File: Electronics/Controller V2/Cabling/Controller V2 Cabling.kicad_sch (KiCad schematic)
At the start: 16 parts, among them J1 776164-1, J10 Autosteer Motor, J11 Battery, J12 776286-1, J13 WAS, J2 GPIO, J3 Tractor CAN, J4 Scraper CAN, J5 Spare CAN, J6 Front Height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

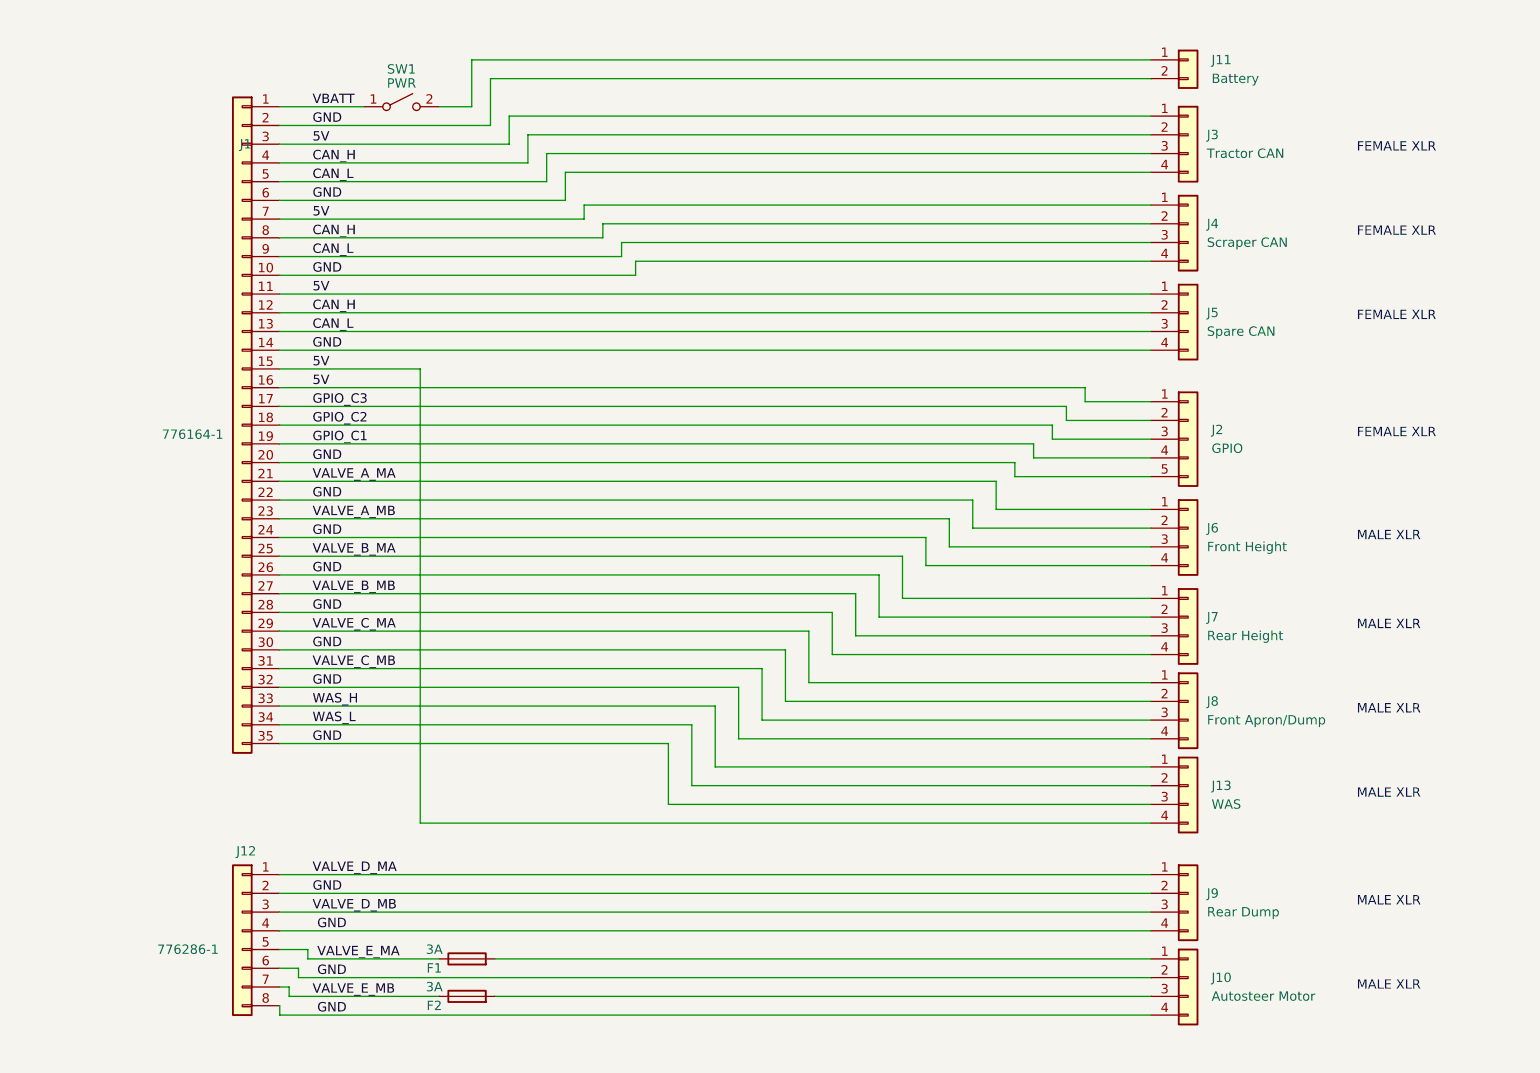
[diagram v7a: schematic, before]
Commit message: Updated controller V2 cabling. Added additional IMU PGNs - not currently used.
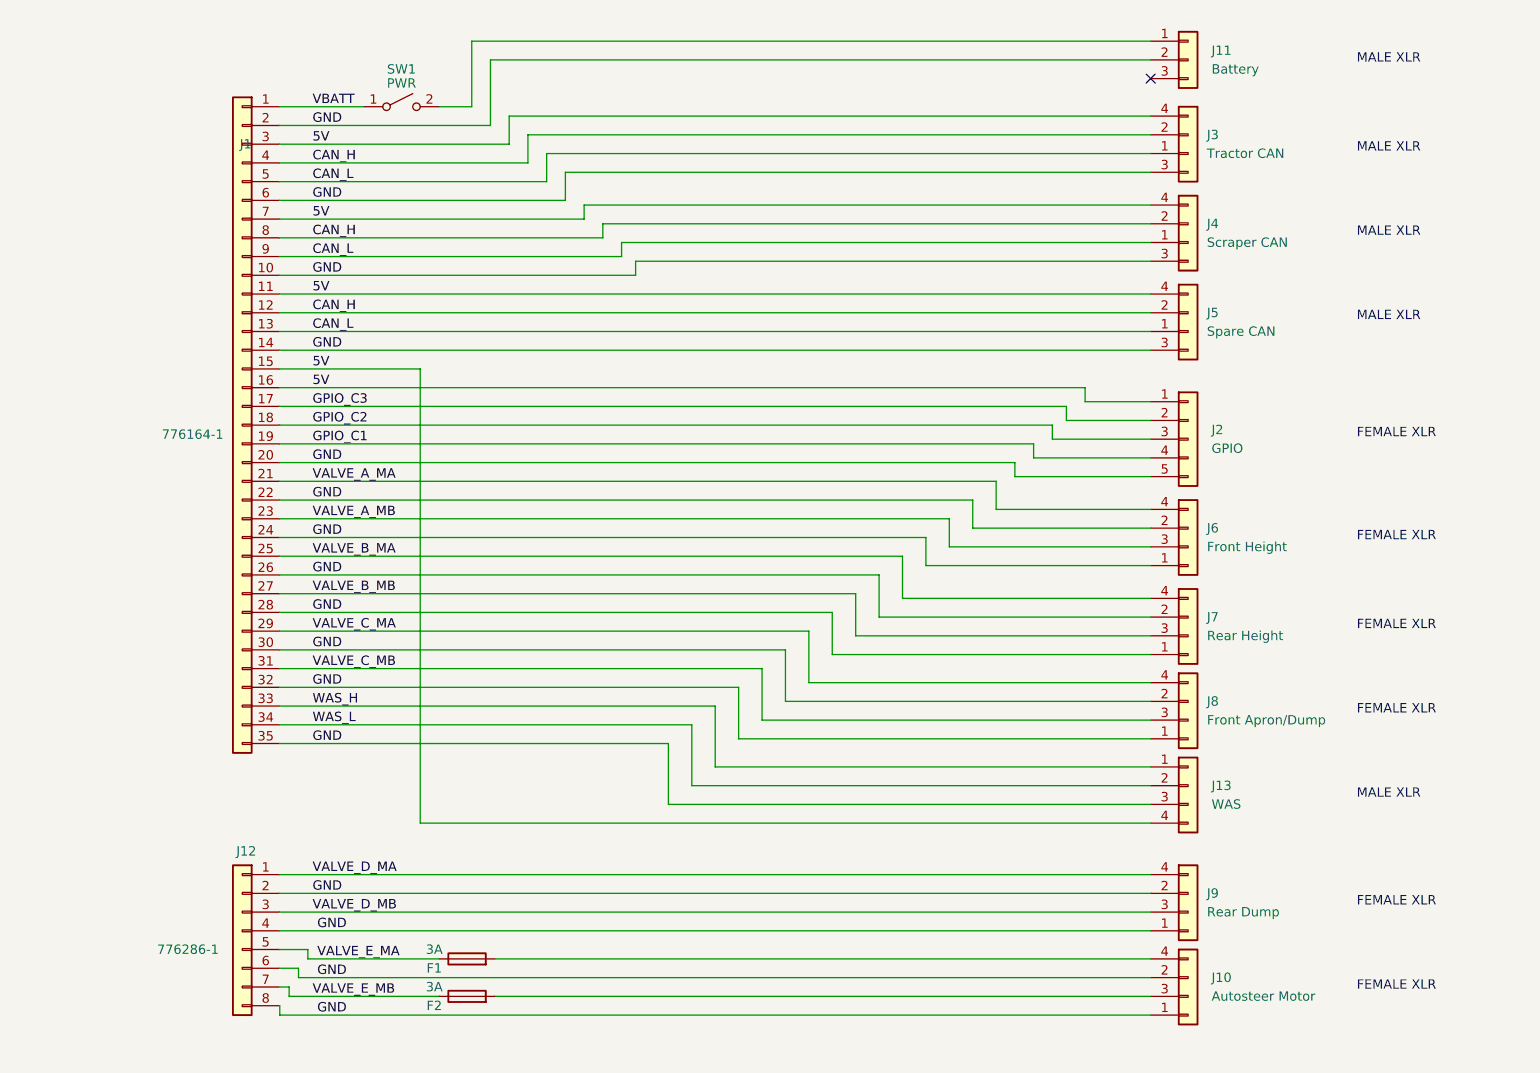
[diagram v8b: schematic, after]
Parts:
- J11: symbol Connector_Generic:Conn_01x02 -> Connector_Generic:Conn_01x03
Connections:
- net 5V: now also J3.4 (Pin_1), J4.4 (Pin_1), J5.4 (Pin_1); no longer J3.1 (Pin_1), J4.1 (Pin_1), J5.1 (Pin_1)
- net CAN_L: now also J3.1 (Pin_3), J4.1 (Pin_3), J5.1 (Pin_3); no longer J3.3 (Pin_3), J4.3 (Pin_3), J5.3 (Pin_3)
- net GND: now also J10.1 (Pin_4), J3.3 (Pin_4), J4.3 (Pin_4), J5.3 (Pin_4), J6.1 (Pin_4), J7.1 (Pin_4), J8.1 (Pin_4), J9.1 (Pin_4); no longer J10.4 (Pin_4), J3.4 (Pin_4), J4.4 (Pin_4), J5.4 (Pin_4), J6.4 (Pin_4), J7.4 (Pin_4), J8.4 (Pin_4), J9.4 (Pin_4)
- net VALVE_A_MA: now also J6.4 (Pin_1); no longer J6.1 (Pin_1)
- net VALVE_B_MA: now also J7.4 (Pin_1); no longer J7.1 (Pin_1)
- net VALVE_C_MA: now also J8.4 (Pin_1); no longer J8.1 (Pin_1)
- net VALVE_D_MA: now also J9.4 (Pin_1); no longer J9.1 (Pin_1)
- net at F1.2: now also J10.4 (Pin_1); no longer J10.1 (Pin_1)
- no-connect marks 0 -> 1
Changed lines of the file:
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@@
   (title_block
     (title "Tandem Leveller Controller V2 Cabling")
-    (date "2026-02-02")
+    (date "2026-04-26")
     (rev "V1.0")
     (company "(C) andy@britishideas.com 2026")
     (comment 1 "NO WARRANTY, SUPPLIED AS-IS")
   )
+  (no_connect (at 202.565 29.845))
   (wire (pts (xy 202.565 116.84) (xy 149.86 116.84))
     (stroke (width 0) (type default))
@@
     (stroke (width 0) (type default))
   )
-  (wire (pts (xy 202.565 29.845) (xy 113.03 29.845))
+  (wire (pts (xy 202.565 27.305) (xy 113.03 27.305))
     (stroke (width 0) (type default))
   )
@@
     (stroke (width 0) (type default))
   )
-  (wire (pts (xy 113.03 29.845) (xy 113.03 36.195))
+  (wire (pts (xy 113.03 27.305) (xy 113.03 36.195))
     (stroke (width 0) (type default))
   )
@@
     (stroke (width 0) (type default))
   )
-  (wire (pts (xy 110.49 27.305) (xy 110.49 33.655))
+  (wire (pts (xy 110.49 24.765) (xy 110.49 33.655))
     (stroke (width 0) (type default))
   )
@@
     (stroke (width 0) (type default))
   )
-  (wire (pts (xy 110.49 27.305) (xy 202.565 27.305))
+  (wire (pts (xy 110.49 24.765) (xy 202.565 24.765))
     (stroke (width 0) (type default))
   )
@@
     (stroke (width 0) (type default))
   )
-  (text "FEMALE XLR" (at 230.505 40.005 0)
-    (effects (font (size 1.27 1.27)) (justify left bottom))
-  )
-  (text "FEMALE XLR" (at 230.505 51.435 0)
-    (effects (font (size 1.27 1.27)) (justify left bottom))
-  )
-  (text "MALE XLR" (at 230.505 153.67 0)
-    (effects (font (size 1.27 1.27)) (justify left bottom))
-  )
-  (text "MALE XLR" (at 230.505 92.71 0)
-    (effects (font (size 1.27 1.27)) (justify left bottom))
-  )
-  (text "MALE XLR" (at 230.505 104.775 0)
+  (text "MALE XLR" (at 230.505 27.94 0)
+    (effects (font (size 1.27 1.27)) (justify left bottom))
+  )
+  (text "MALE XLR" (at 230.505 40.005 0)
+    (effects (font (size 1.27 1.27)) (justify left bottom))
+  )
+  (text "MALE XLR" (at 230.505 51.435 0)
+    (effects (font (size 1.27 1.27)) (justify left bottom))
+  )
+  (text "FEMALE XLR" (at 230.505 153.67 0)
+    (effects (font (size 1.27 1.27)) (justify left bottom))
+  )
+  (text "FEMALE XLR" (at 230.505 92.71 0)
+    (effects (font (size 1.27 1.27)) (justify left bottom))
+  )
+  (text "FEMALE XLR" (at 230.505 104.775 0)
     (effects (font (size 1.27 1.27)) (justify left bottom))
   )
@@
     (effects (font (size 1.27 1.27)) (justify left bottom))
   )
-  (text "MALE XLR" (at 230.505 142.24 0)
+  (text "FEMALE XLR" (at 230.505 142.24 0)
     (effects (font (size 1.27 1.27)) (justify left bottom))
   )
@@
     (effects (font (size 1.27 1.27)) (justify left bottom))
   )
-  (text "MALE XLR" (at 230.505 116.205 0)
-    (effects (font (size 1.27 1.27)) (justify left bottom))
-  )
-  (text "FEMALE XLR" (at 230.505 62.865 0)
+  (text "FEMALE XLR" (at 230.505 116.205 0)
+    (effects (font (size 1.27 1.27)) (justify left bottom))
+  )
+  (text "MALE XLR" (at 230.505 62.865 0)
     (effects (font (size 1.27 1.27)) (justify left bottom))
   )
@@
     (effects (font (size 1.27 1.27)) (justify left bottom))
   )
-  (symbol (lib_id "Connector_Generic:Conn_01x04") (at 207.645 49.53 0) (unit 1)
+  (symbol (lib_name "Conn_01x04_2") (lib_id "Connector_Generic:Conn_01x04") (at 207.645 49.53 0) (unit 1)
     (in_bom yes) (on_board yes) (dnp no) (fields_autoplaced)
     (property "Reference" "J4" (at 210.185 49.53 0)
@@
     )
   )
-  (symbol (lib_id "Connector_Generic:Conn_01x04") (at 207.645 37.465 0) (unit 1)
+  (symbol (lib_name "Conn_01x04_1") (lib_id "Connector_Generic:Conn_01x04") (at 207.645 37.465 0) (unit 1)
     (in_bom yes) (on_board yes) (dnp no) (fields_autoplaced)
     (property "Reference" "J3" (at 210.185 37.465 0)
@@
     )
   )
-  (symbol (lib_id "Connector_Generic:Conn_01x04") (at 207.645 102.87 0) (unit 1)
+  (symbol (lib_name "Conn_01x04_5") (lib_id "Connector_Generic:Conn_01x04") (at 207.645 102.87 0) (unit 1)
     (in_bom yes) (on_board yes) (dnp no) (fields_autoplaced)
     (property "Reference" "J7" (at 210.185 102.87 0)
@@
     )
   )
-  (symbol (lib_id "Connector_Generic:Conn_01x04") (at 207.645 90.805 0) (unit 1)
+  (symbol (lib_name "Conn_01x04_4") (lib_id "Connector_Generic:Conn_01x04") (at 207.645 90.805 0) (unit 1)
     (in_bom yes) (on_board yes) (dnp no) (fields_autoplaced)
     (property "Reference" "J6" (at 210.185 90.805 0)
@@
     )
   )
-  (symbol (lib_id "Connector_Generic:Conn_01x04") (at 207.645 140.335 0) (unit 1)
+  (symbol (lib_name "Conn_01x04_7") (lib_id "Connector_Generic:Conn_01x04") (at 207.645 140.335 0) (unit 1)
     (in_bom yes) (on_board yes) (dnp no) (fields_autoplaced)
     (property "Reference" "J9" (at 210.185 140.335 0)
@@
     )
   )
-  (symbol (lib_id "Connector_Generic:Conn_01x04") (at 207.645 151.765 0) (unit 1)
+  (symbol (lib_name "Conn_01x04_8") (lib_id "Connector_Generic:Conn_01x04") (at 207.645 151.765 0) (unit 1)
     (in_bom yes) (on_board yes) (dnp no) (fields_autoplaced)
     (property "Reference" "J10" (at 210.82 151.765 0)
@@
     )
   )
-  (symbol (lib_id "Connector_Generic:Conn_01x04") (at 207.645 114.3 0) (unit 1)
+  (symbol (lib_name "Conn_01x04_6") (lib_id "Connector_Generic:Conn_01x04") (at 207.645 114.3 0) (unit 1)
     (in_bom yes) (on_board yes) (dnp no) (fields_autoplaced)
     (property "Reference" "J8" (at 210.185 114.3 0)
@@
     )
   )
-  (symbol (lib_id "Connector_Generic:Conn_01x02") (at 207.645 27.305 0) (unit 1)
-    (in_bom yes) (on_board yes) (dnp no) (fields_autoplaced)
-    (property "Reference" "J11" (at 210.82 27.305 0)
-      (effects (font (size 1.27 1.27)) (justify left))
-    )
-    (property "Value" "Battery" (at 210.82 29.845 0)
+  (symbol (lib_id "Connector_Generic:Conn_01x03") (at 207.645 27.305 0) (unit 1)
+    (in_bom yes) (on_board yes) (dnp no) (fields_autoplaced)
+    (property "Reference" "J11" (at 210.82 26.035 0)
+      (effects (font (size 1.27 1.27)) (justify left))
+    )
+    (property "Value" "Battery" (at 210.82 28.575 0)
       (effects (font (size 1.27 1.27)) (justify left))
     )
@@
     (pin "1")
     (pin "2")
+    (pin "3")
     (instances
       (project "Controller V2 Cabling"
@@
     )
   )
-  (symbol (lib_id "Connector_Generic:Conn_01x04") (at 207.645 61.595 0) (unit 1)
+  (symbol (lib_name "Conn_01x04_3") (lib_id "Connector_Generic:Conn_01x04") (at 207.645 61.595 0) (unit 1)
     (in_bom yes) (on_board yes) (dnp no) (fields_autoplaced)
     (property "Reference" "J5" (at 210.185 61.595 0)
